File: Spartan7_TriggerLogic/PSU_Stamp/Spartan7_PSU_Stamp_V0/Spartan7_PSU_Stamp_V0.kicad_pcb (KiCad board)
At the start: 4 copper layers, 54.8 x 55.8 mm, 37 parts, among them J1 USB4125-GF-A, U1 LT3081EDF-TRPBF, U2 LT3081EDF-TRPBF, U3 TPS7A8801RTJT, U4 TPS7A8801RTJT

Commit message: .
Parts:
- moved C12 31.2 mm to (128.9, 91.9), turned to 180 degrees
- moved C8 28.0 mm to (126.9, 88.7), turned to 180 degrees
- moved C14 27.9 mm to (132.6, 91.9)
- moved C10 26.0 mm to (134.6, 88.7)
- moved C16 19.1 mm to (127.6, 84.9), turned to -90 degrees
- moved C18 17.3 mm to (133.9, 84.9), turned to -90 degrees
- moved C20 16.9 mm to (132.1, 83.9), turned to 90 degrees
- moved R4 15.5 mm to (135.4, 84.9), turned to -90 degrees
- moved R6 15.0 mm to (134.6, 87.2)
- moved C22 14.3 mm to (129.6, 83.9), turned to 90 degrees
- moved U4 14.1 mm to (130.8, 88.2), turned to 90 degrees
- moved C15 13.8 mm to (138.8, 79.5)
- moved C7 13.8 mm to (138.8, 74.5)
- moved R3 13.8 mm to (138.8, 84.5)
- moved R5 13.8 mm to (138.8, 87.0)
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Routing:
- net +5V: track 6.74 -> 0.00 mm
- net GND: track 0.00 -> 3.28 mm
- net /3.6V-3.3V/EN_2: track 0.00 -> 0.42 mm, vias 0 -> 1
- added copper zone on F.Cu, net +5V
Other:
- board size 54.8 x 55.8 mm -> 24.3 x 41.5 mm

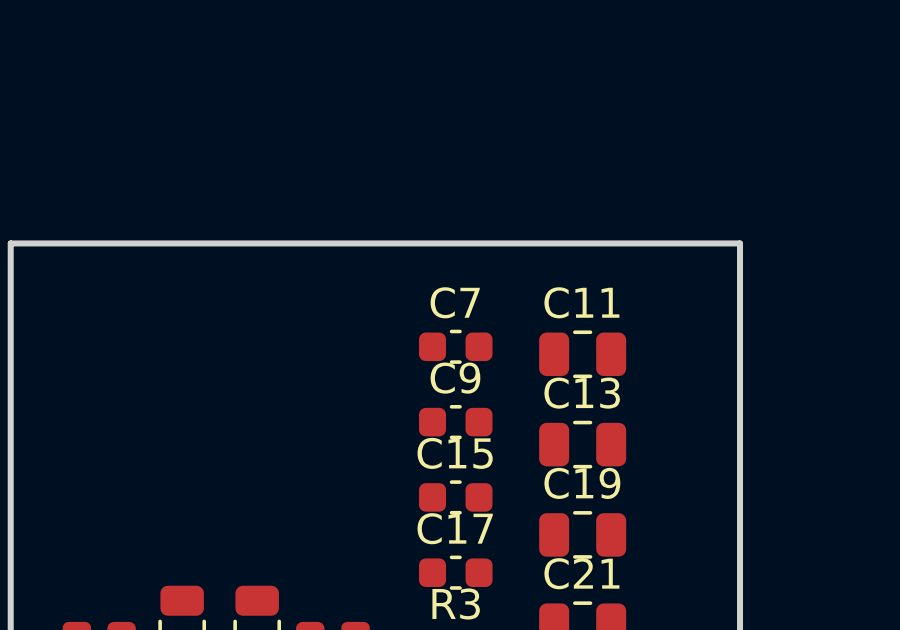
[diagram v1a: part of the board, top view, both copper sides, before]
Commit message: Adjust C7 footprint position on PSU Stamp PCB
Moved the C7 capacitor footprint to new coordinates (138.38, 74.27) on the Spartan7_PSU_Stamp_V0.kicad_pcb file for improved layout. Updated backup ZIP to reflect latest PCB changes.
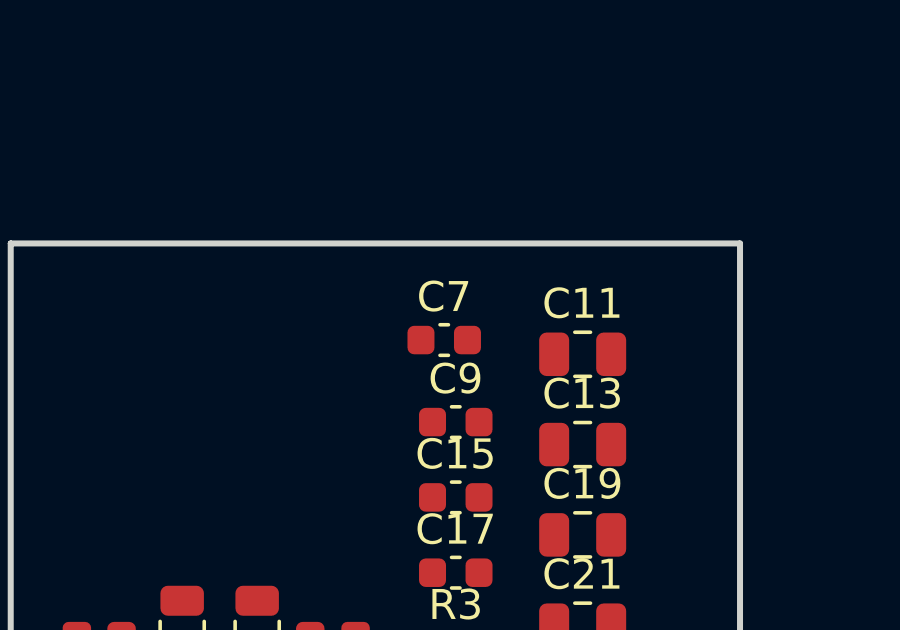
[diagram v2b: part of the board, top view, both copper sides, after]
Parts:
- moved C7 0.45 mm to (138.4, 74.3)
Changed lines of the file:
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@@
 	(footprint "Capacitor_SMD:C_0603_1608Metric"
 		(layer "F.Cu")
-		(at 138.764999 74.494999)
+		(at 138.38 74.27)
 		(descr "Capacitor SMD 0603 (1608 Metric), square (rectangular) end terminal, IPC-7351 nominal, (Body size source: IPC-SM-782 page 76, https://www.pcb-3d.com/wordpress/wp-content/uploads/ipc-sm-782a_amendment_1_and_2.pdf), generated with kicad-footprint-generator")
 		(tags "capacitor")

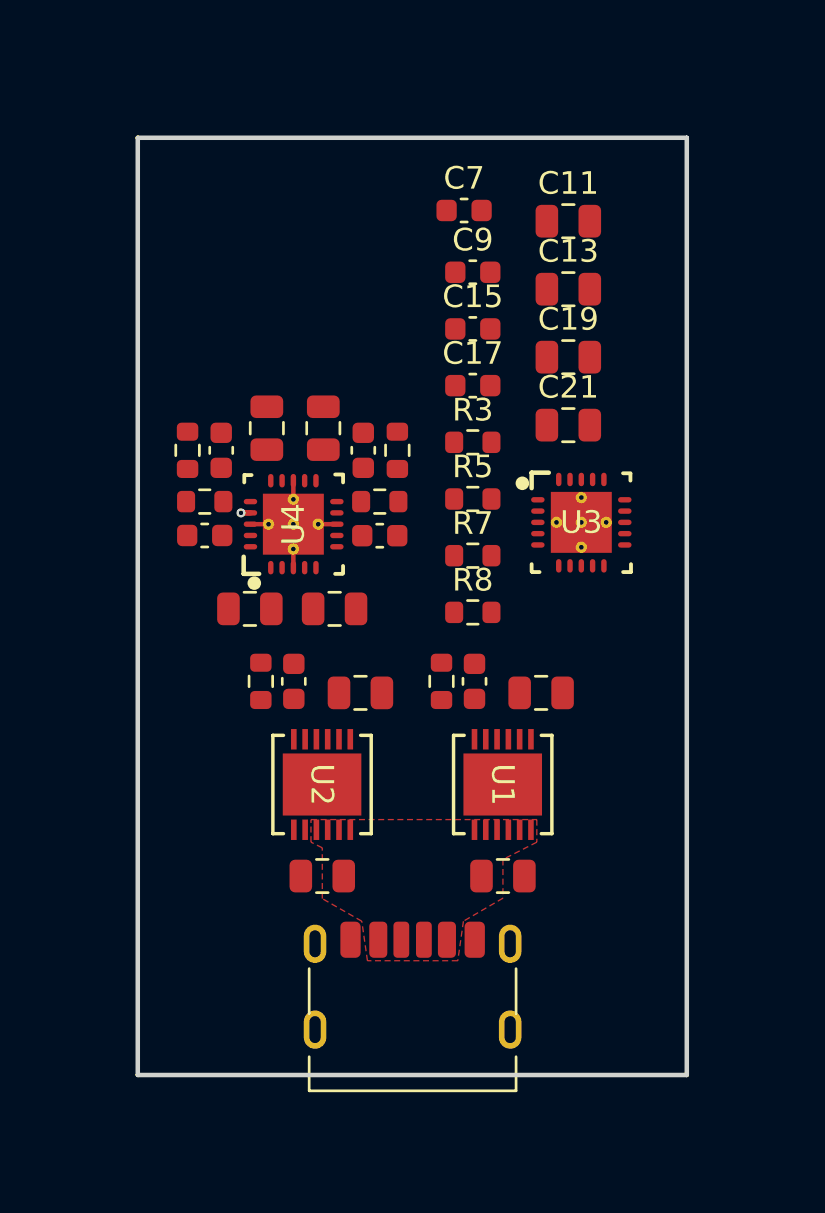
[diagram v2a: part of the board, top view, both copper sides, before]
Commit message: Add USB-C power and TPS7A2033PDBVR symbol
Added USB_C_Power schematic, new TPS7A2033PDBVR symbol and library, and updated net names and layout for improved clarity. Also included new backup files and made minor footprint and netlist adjustments for the Spartan7 PSU Stamp project.
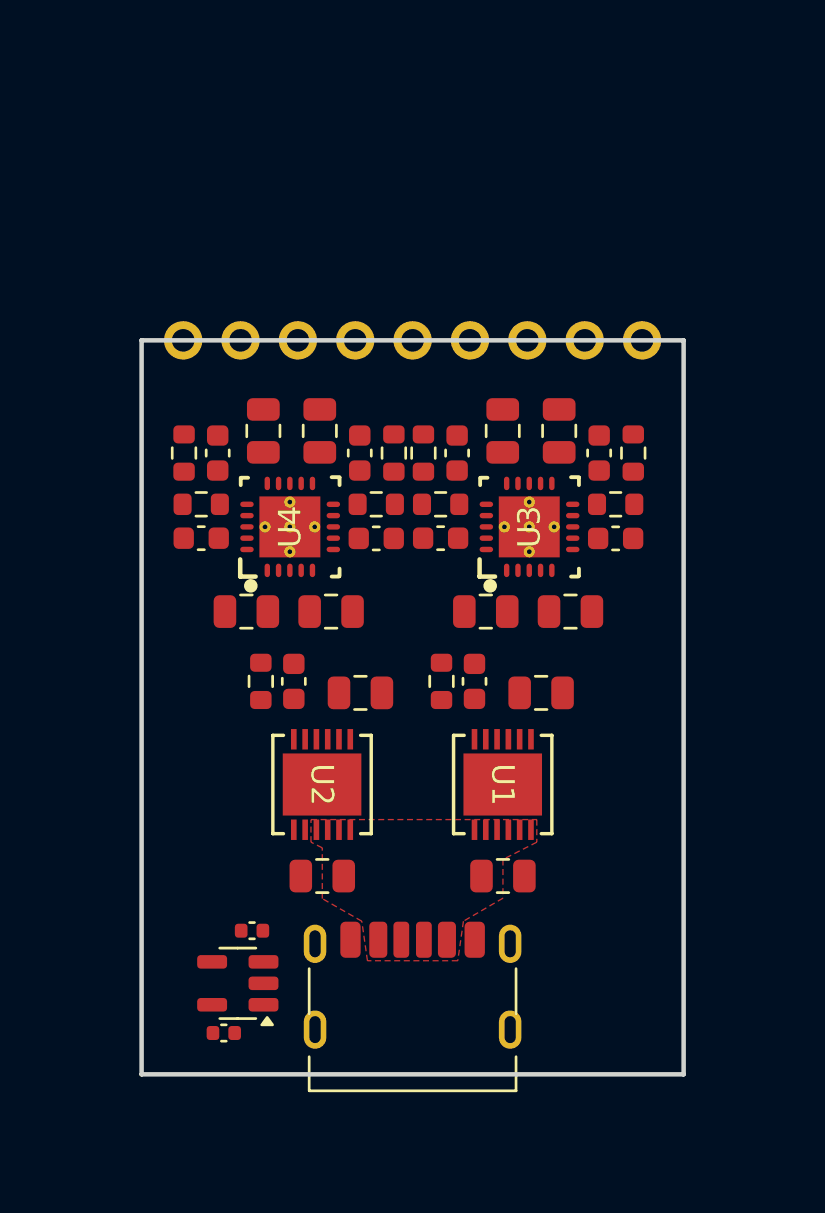
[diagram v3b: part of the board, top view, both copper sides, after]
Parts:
- added C23: 1u, Capacitor_SMD:C_0402_1005Metric, F.Cu at (129.0, 106.2)
- added C24: 1u, Capacitor_SMD:C_0402_1005Metric, F.Cu at (127.7, 110.7)
- added J2: Castellated_holes, Connector_PinHeader_2.54mm:PinHeader_1x09_P2.54mm_Vertical, F.Cu at (125.9, 80.0)
- added U5: TPS7A2033, Package_TO_SOT_SMD:SOT-23-5, F.Cu at (128.4, 108.5)
- moved C11 17.7 mm to (139.3, 92.0), turned to 180 degrees
- moved C7 14.5 mm to (137.3, 88.8), turned to 180 degrees
- moved C13 14.3 mm to (143.1, 92.0)
- moved C9 13.4 mm to (145.1, 88.8)
- moved R3 7.12 mm to (145.9, 85.0), turned to -90 degrees
- moved C17 6.34 mm to (144.4, 85.0), turned to -90 degrees
- moved R5 6.33 mm to (145.1, 87.3)
- moved C15 5.54 mm to (138.1, 85.0), turned to -90 degrees
- moved R7 5.04 mm to (136.6, 85.0), turned to -90 degrees
- moved R8 4.99 mm to (137.3, 87.3), turned to 180 degrees
- moved C19 3.29 mm to (142.6, 84.0), turned to 90 degrees
- moved C21 2.92 mm to (140.1, 84.0), turned to 90 degrees
- moved U3 2.31 mm to (141.3, 88.3), turned to 90 degrees
- moved C10 0.20 mm to (134.5, 88.8)
- moved C12 0.20 mm to (128.7, 92.0)
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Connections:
- net /2.5V-1.8V and 1V/EN_1 renamed /2.5V to 1V and 1.8V/EN_1
- net /2.5V-1.8V and 1V/V_out_1 renamed /V_core_1V
- net /2.5V-1.8V and 1V/V_out_2 renamed /V_aux_1V8
- net /3.6V-3.3V/V_in renamed /3.6V to 3.3V/V_in
- net /3.6V-3.3V/V_out_1 renamed /V_Bank_14_3V3
- net /3.6V-3.3V/V_out_2 renamed /V_Bank_34_3V3
- U3 pad 17: /2.5V-1.8V and 1V/EN_2 -> /2.5V to 1V and 1.8V/PG_1
- U3 pad 6: /2.5V-1.8V and 1V/EN_2 -> /2.5V to 1V and 1.8V/EN_2
- U3 pad 9: /2.5V-1.8V and 1V/PG_2 -> /2.5V to 1V and 1.8V/PG_2
- U4 pad 17: /3.6V-3.3V/EN_2 -> /3.6V to 3.3V/PG_1
- U4 pad 20: /2.5V-1.8V and 1V/PG_2 -> /3.6V to 3.3V/EN_1
- U4 pad 6: /3.6V-3.3V/EN_2 -> /3.6V to 3.3V/EN_2
- U4 pad 9: /3.6V-3.3V/PG_2 -> /DONE_0
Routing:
- net GND: track 3.28 -> 0.00 mm
- net /3.6V-3.3V/EN_2: track 0.42 -> 0.00 mm, vias 1 -> 0
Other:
- board size 24.3 x 41.5 mm -> 24 x 32.5 mm

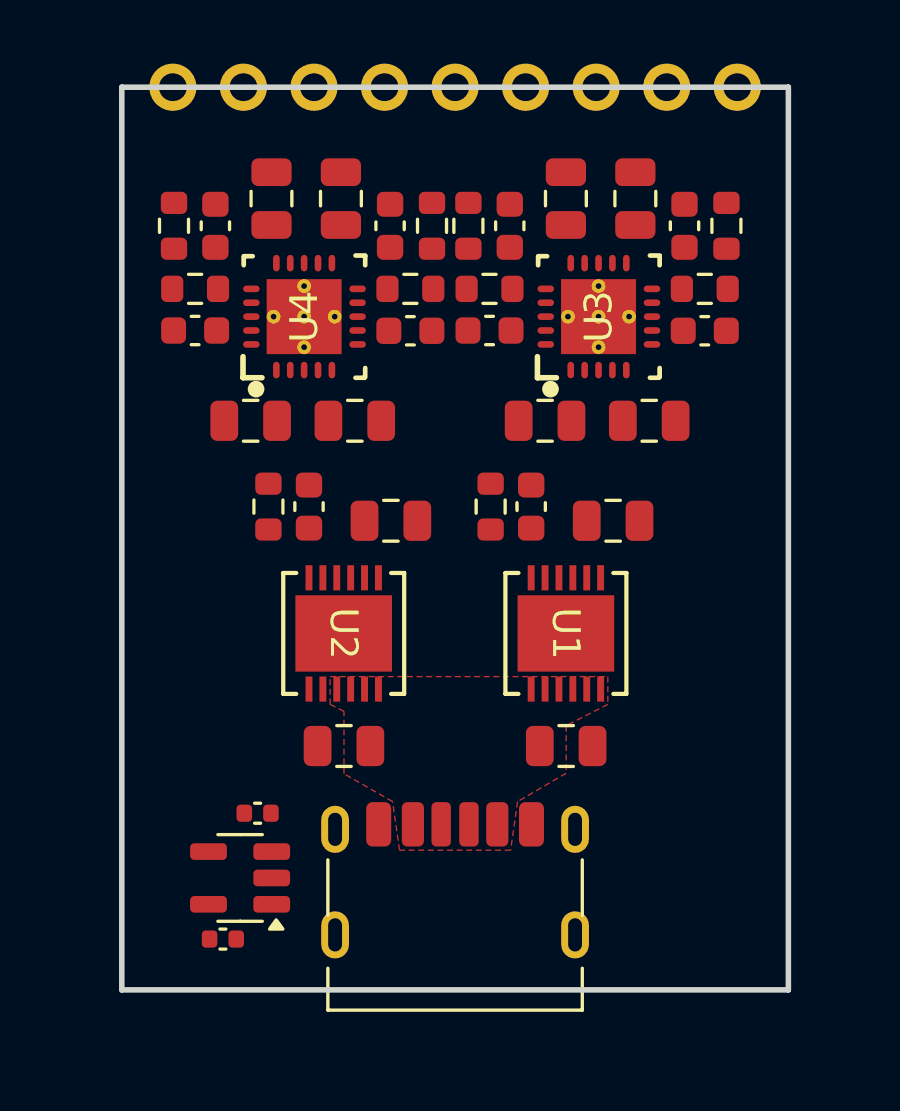
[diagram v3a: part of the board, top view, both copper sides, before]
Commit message: Update net assignments and add vias in KiCad PCB
Reassigned several net numbers and names in Spartan7_PSU_Stamp_V0.kicad_pcb for improved clarity and consistency. Added multiple via definitions and updated related PCB segments. Removed old backup files and added new ones to the backups directory.
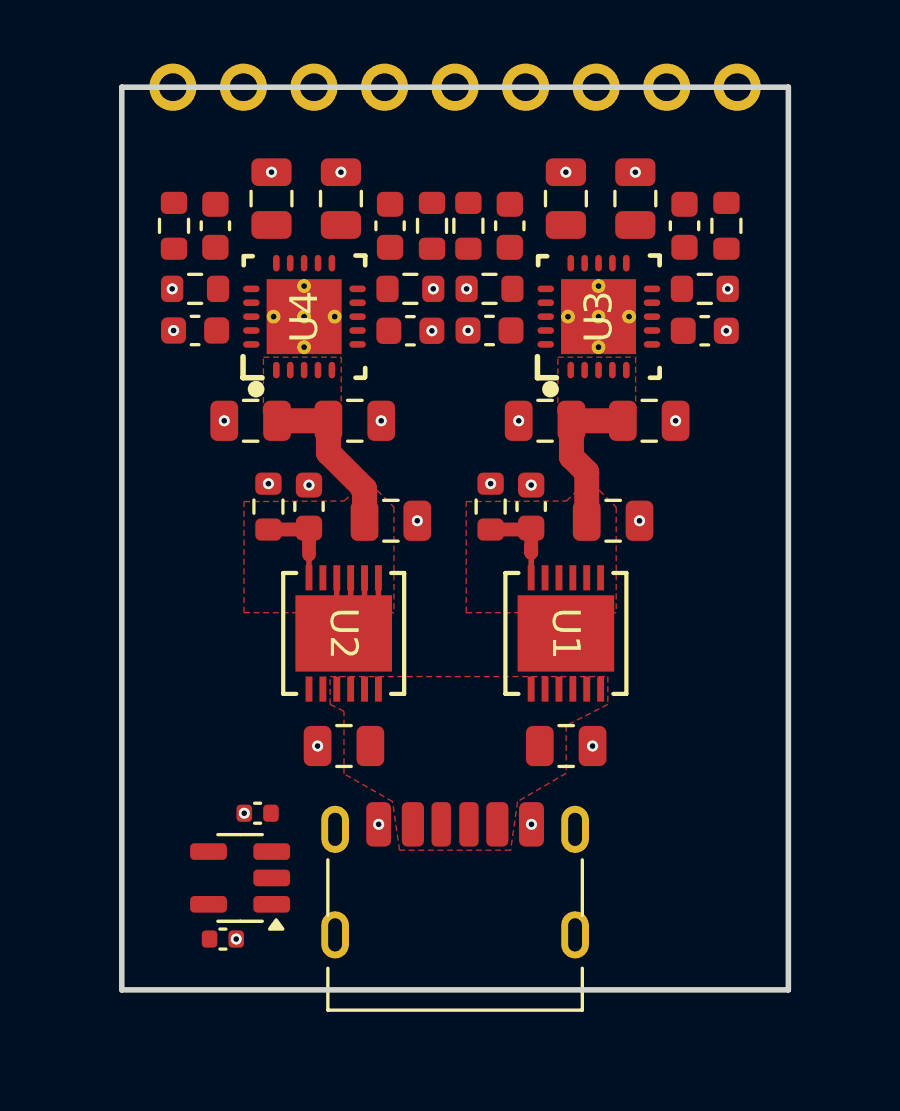
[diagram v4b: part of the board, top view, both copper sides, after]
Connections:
- net /2.5V to 1V and 1.8V/EN_1 renamed /2V5
- net /3.6V to 3.3V/V_in renamed /3V6
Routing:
- net /3V6: track 0.00 -> 15.0 mm
- net /2V5: track 0.00 -> 5.68 mm
- net Net-(U1-SET): track 0.00 -> 3.73 mm
- net Net-(U2-SET): track 0.00 -> 3.24 mm
- net GND: vias 0 -> 28
- added copper zone on F.Cu, net /2V5
- added copper zone on F.Cu, net /3V6

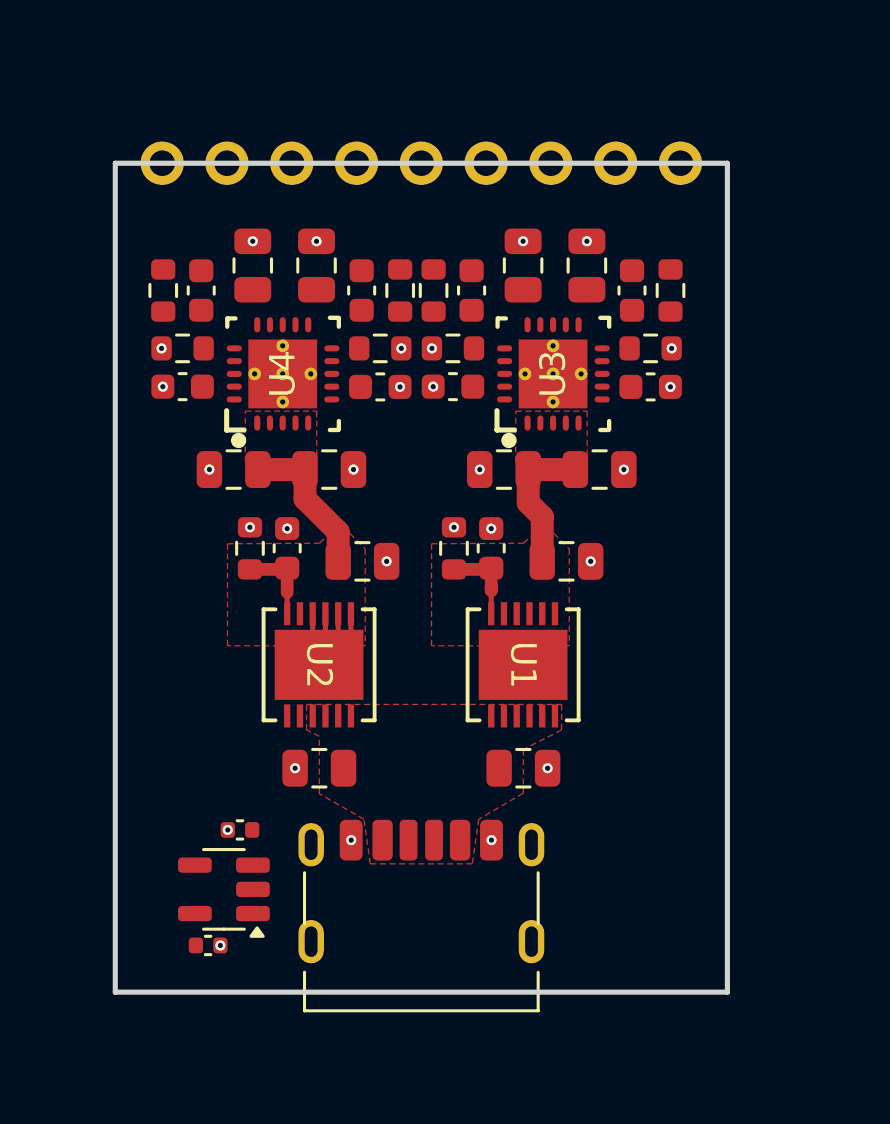
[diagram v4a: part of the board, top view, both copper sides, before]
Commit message: Add status LEDs and update power nets
Added new 0402 LEDs (D1, D4) and supporting resistor (R12) for power-good status indication. Updated net assignments and replaced a capacitor footprint with an LED. Modified schematic and PCB files to reflect these changes.
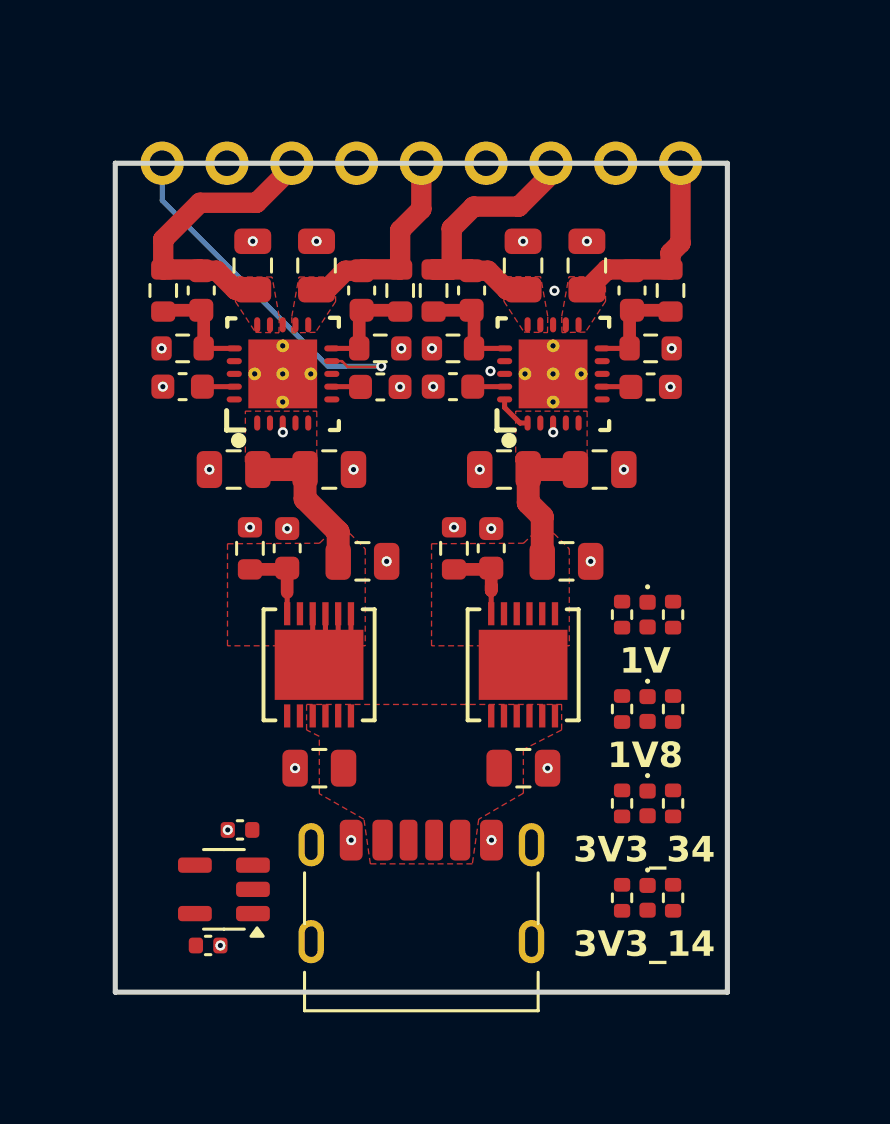
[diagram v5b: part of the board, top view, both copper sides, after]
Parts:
- added D1: 1V_ok, LED_SMD:LED_0402_1005Metric, F.Cu at (145.0, 97.7)
- added D2: 1V_ok, LED_SMD:LED_0402_1005Metric, F.Cu at (145.0, 101.4)
- added D3: 1V_ok, LED_SMD:LED_0402_1005Metric, F.Cu at (145.0, 108.8)
- added D4: 1V_ok, LED_SMD:LED_0402_1005Metric, F.Cu at (145.0, 105.1)
- added R11: 10k, Resistor_SMD:R_0402_1005Metric, F.Cu at (144.0, 97.7)
- added R12: 680, Resistor_SMD:R_0402_1005Metric, F.Cu at (146.0, 97.7)
- added R13: 680, Resistor_SMD:R_0402_1005Metric, F.Cu at (146.0, 101.4)
- added R14: 10k, Resistor_SMD:R_0402_1005Metric, F.Cu at (144.0, 101.4)
- added R15: 680, Resistor_SMD:R_0402_1005Metric, F.Cu at (146.0, 108.8)
- added R16: 10k, Resistor_SMD:R_0402_1005Metric, F.Cu at (144.0, 108.8)
- added R17: 680, Resistor_SMD:R_0402_1005Metric, F.Cu at (146.0, 105.1)
- added R18: 10k, Resistor_SMD:R_0402_1005Metric, F.Cu at (144.0, 105.1)
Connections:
- U3 pad 17: /2.5V to 1V and 1.8V/PG_1 -> /PG_1V_ok
- U3 pad 6: /2.5V to 1V and 1.8V/EN_2 -> /PG_1V_ok
- U3 pad 9: /2.5V to 1V and 1.8V/PG_2 -> /PG_1V8_ok
- U4 pad 17: /3.6V to 3.3V/PG_1 -> /PG_3V3_14_ok
- U4 pad 20: /3.6V to 3.3V/EN_1 -> /PG_1V8_ok
- U4 pad 6: /3.6V to 3.3V/EN_2 -> /PG_3V3_14_ok
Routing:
- net /DONE_0: track 0.00 -> 14.8 mm, vias 0 -> 1
- net /V_Bank_14_3V3: track 0.00 -> 11.4 mm
- net /V_core_1V: track 0.00 -> 11.4 mm
- net /V_Bank_34_3V3: track 0.00 -> 8.12 mm
- net /V_aux_1V8: track 0.00 -> 7.94 mm
- net Net-(U3-FB1): track 0.00 -> 4.25 mm
- net Net-(U4-FB1): track 0.00 -> 4.25 mm
- net Net-(U4-FB2): track 0.00 -> 4.14 mm
- net Net-(U3-FB2): track 0.00 -> 4.14 mm
- net /2V5: track 5.68 -> 7.15 mm
- net Net-(U3-NR_SS1): track 0.00 -> 1.25 mm
- net Net-(U4-NR_SS1): track 0.00 -> 1.25 mm
- net Net-(U4-NR_SS2): track 0.00 -> 1.13 mm
- net Net-(U3-NR_SS2): track 0.00 -> 1.13 mm
- net GND: vias 28 -> 32
- added copper zone on F.Cu, net /V_Bank_14_3V3
- added copper zone on F.Cu, net /V_Bank_34_3V3
- added copper zone on F.Cu, net /V_aux_1V8
- added copper zone on F.Cu, net /V_core_1V
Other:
- board text added: "1V"
- board text added: "1V8"
- board text added: "3V3_14"
- board text added: "3V3_34"
